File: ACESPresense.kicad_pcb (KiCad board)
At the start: 2 copper layers, 95.1 x 48 mm, 17 parts, among them U1 ESP32-WROOM-32D

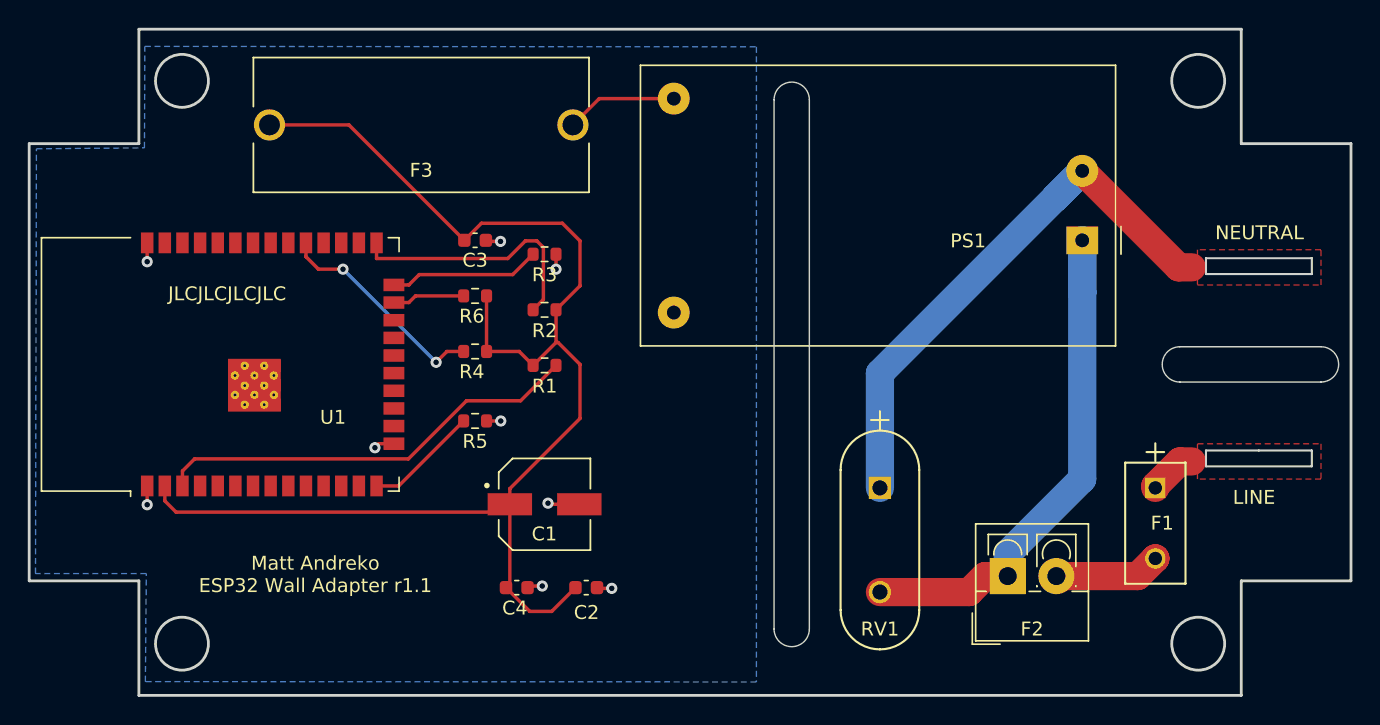
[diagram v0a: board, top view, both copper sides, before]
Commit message: Added test points and fixed file names internally
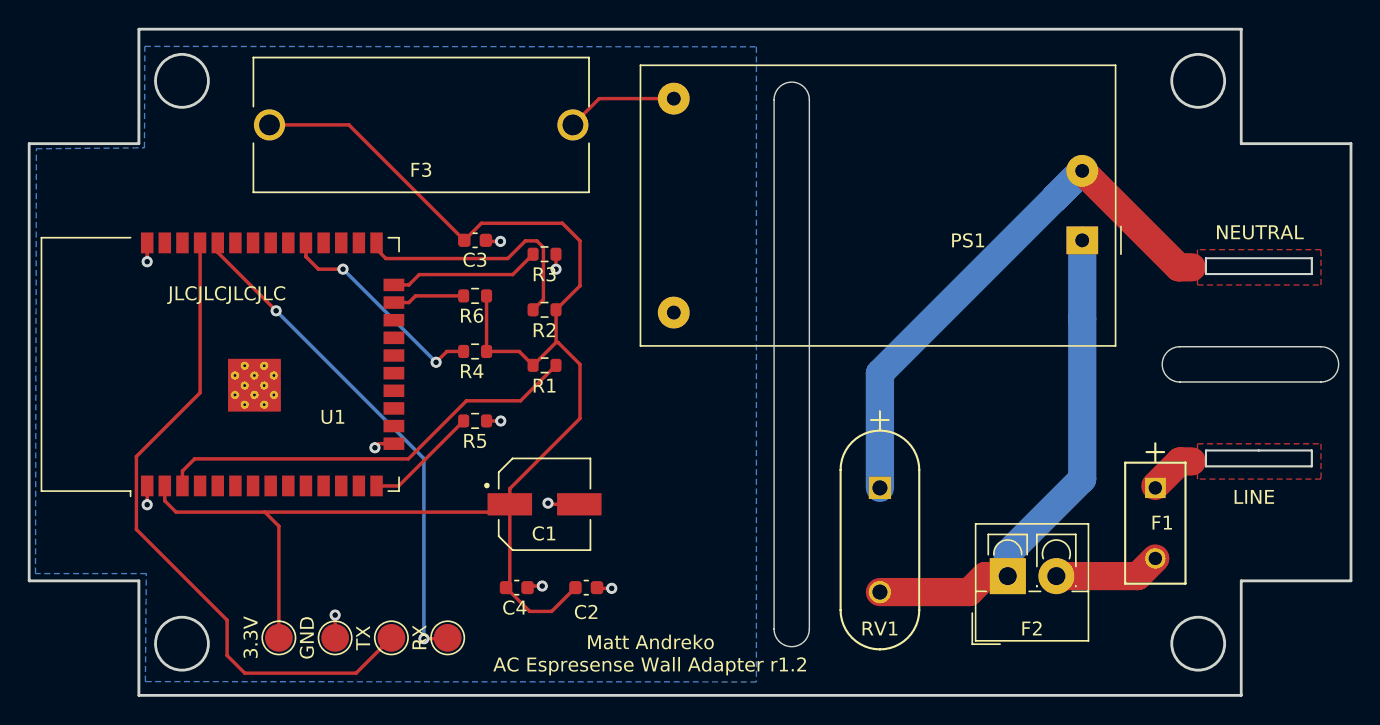
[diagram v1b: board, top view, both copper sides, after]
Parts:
- added 3.3V: TestPoint, TestPoint:TestPoint_Pad_D2.0mm, F.Cu at (60.9, 94.6)
- added GND: TestPoint, TestPoint:TestPoint_Pad_D2.0mm, F.Cu at (64.9, 94.6)
- added RX: TestPoint, TestPoint:TestPoint_Pad_D2.0mm, F.Cu at (73.0, 94.6)
- added TX: TestPoint, TestPoint:TestPoint_Pad_D2.0mm, F.Cu at (69.0, 94.6)
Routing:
- net /TX: track 0.00 -> 47.7 mm
- net /RX: track 0.00 -> 36.4 mm, vias 0 -> 2
- net +3.3V: track 98.3 -> 107.7 mm
- net Net-(PS1-AC/L): track 39.8 -> 36.1 mm
- net GND: track 18.2 -> 19.8 mm, vias 9 -> 10
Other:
- board text added: "Matt Andreko AC Espresense Wall Adapter r1.2"
- board text removed: "Matt Andreko ESP32 Wall Adapter r1.1"
